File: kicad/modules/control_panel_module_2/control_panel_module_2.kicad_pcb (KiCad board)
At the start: 2 copper layers, 75 x 28 mm, 21 parts, among them J1 Screw_Terminal_01x06, J2 Screw_Terminal_01x06, U1 ULN2004A

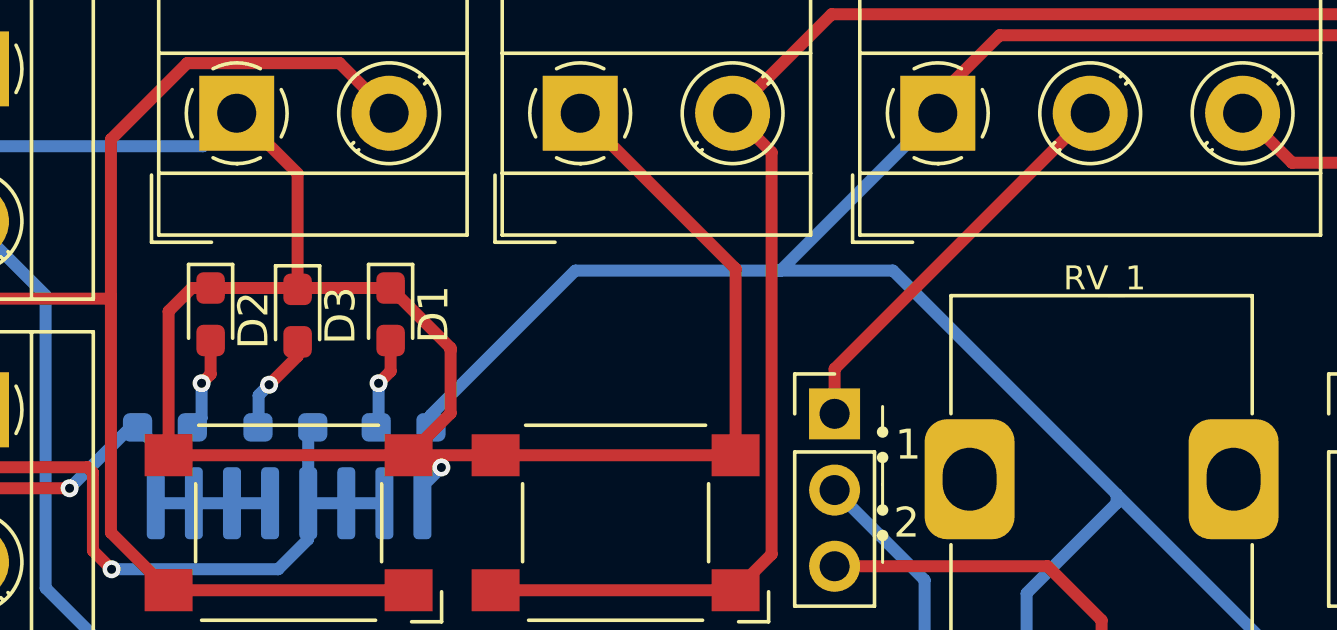
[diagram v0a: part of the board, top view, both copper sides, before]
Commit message: LED footprint update
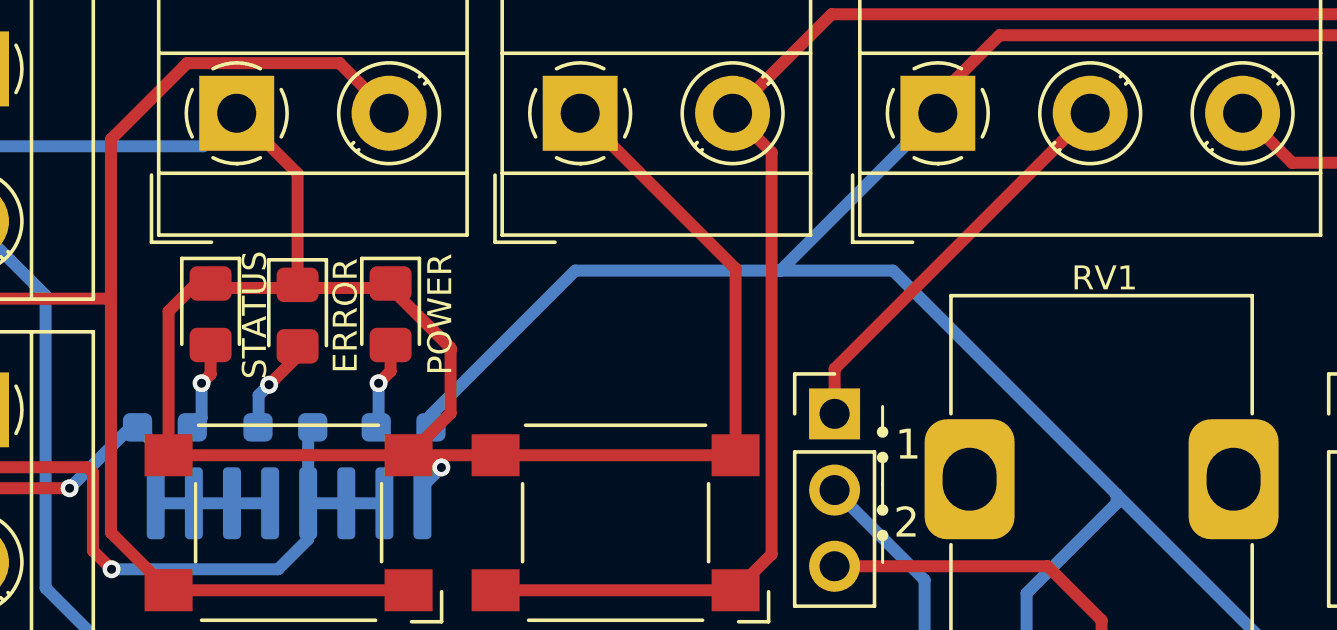
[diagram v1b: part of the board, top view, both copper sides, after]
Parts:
- ERROR: renamed from D3; footprint LED_SMD:LED_0603_1608Metric_Pad1.05x0.95mm_HandSolder -> LED_SMD:LED_0805_2012Metric_Pad1.15x1.40mm_HandSolder
- J1, J2: value Screw_Terminal_01x06 -> 1x6 2.54
- J3: renamed from RV_1; value ~ -> 1x3 5.08
- J5: renamed from SW_1; value ~ -> 1x2 5.08
- J7: renamed from LED_STATUS_OFFBOARD1; value ~ -> 1x2 5.08
- J8: renamed from LED_ERR_OFFBOARD1; value ~ -> 1x2 5.08
- JP1, JP2: value Jumper_3_Bridged12 -> 1x3 2.54
- POWER: renamed from D1; footprint LED_SMD:LED_0603_1608Metric_Pad1.05x0.95mm_HandSolder -> LED_SMD:LED_0805_2012Metric_Pad1.15x1.40mm_HandSolder
- RV_2: value ~ -> 1x3 5.08
- STATUS: renamed from D2; footprint LED_SMD:LED_0603_1608Metric_Pad1.05x0.95mm_HandSolder -> LED_SMD:LED_0805_2012Metric_Pad1.15x1.40mm_HandSolder
- SW_2: value ~ -> 1x2 5.08
- renumbered RV_1 to RV1, RV_SPEED4 to RV2, SWITCH_2 to SW2
